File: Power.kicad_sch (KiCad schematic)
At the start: 17 parts, among them U6 TLV61070A, U9 AP2210K-3.3TRG1

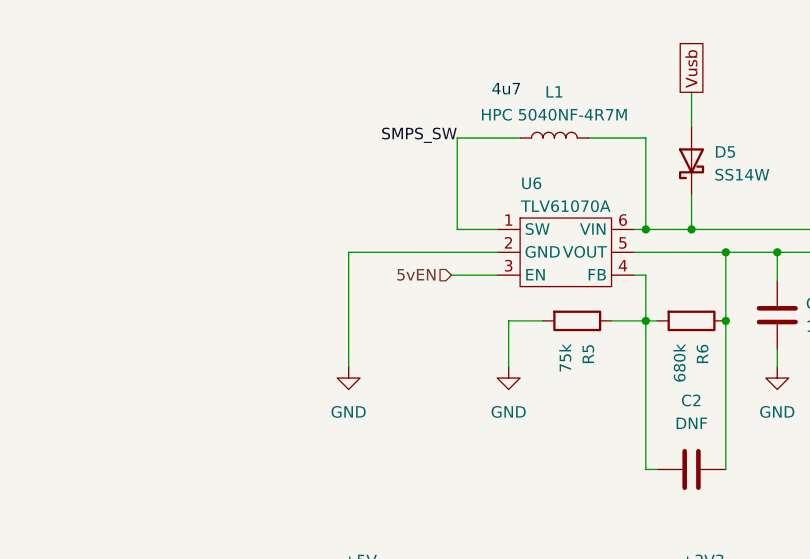
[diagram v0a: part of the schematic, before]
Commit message: Begin screen module
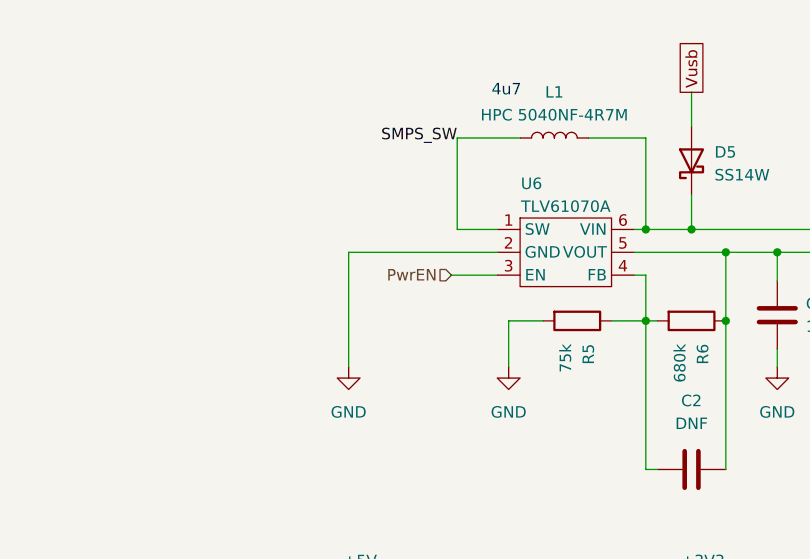
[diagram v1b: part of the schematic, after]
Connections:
- net 5vEN renamed PwrEN
